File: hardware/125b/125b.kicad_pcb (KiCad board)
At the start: 2 copper layers, 59 x 75 mm, 49 parts, among them J1 Guitar in, J2 Barrel_Jack, J3 Conn_02x05_Odd_Even_MountingP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, J4 Guitar out, SW1 SW_Push_SPDT, SW2 RotaryEncoder_Switch, SW3 SW_Push, SW4 SW_Push, U1 L78L05_TO92, U2 TL074

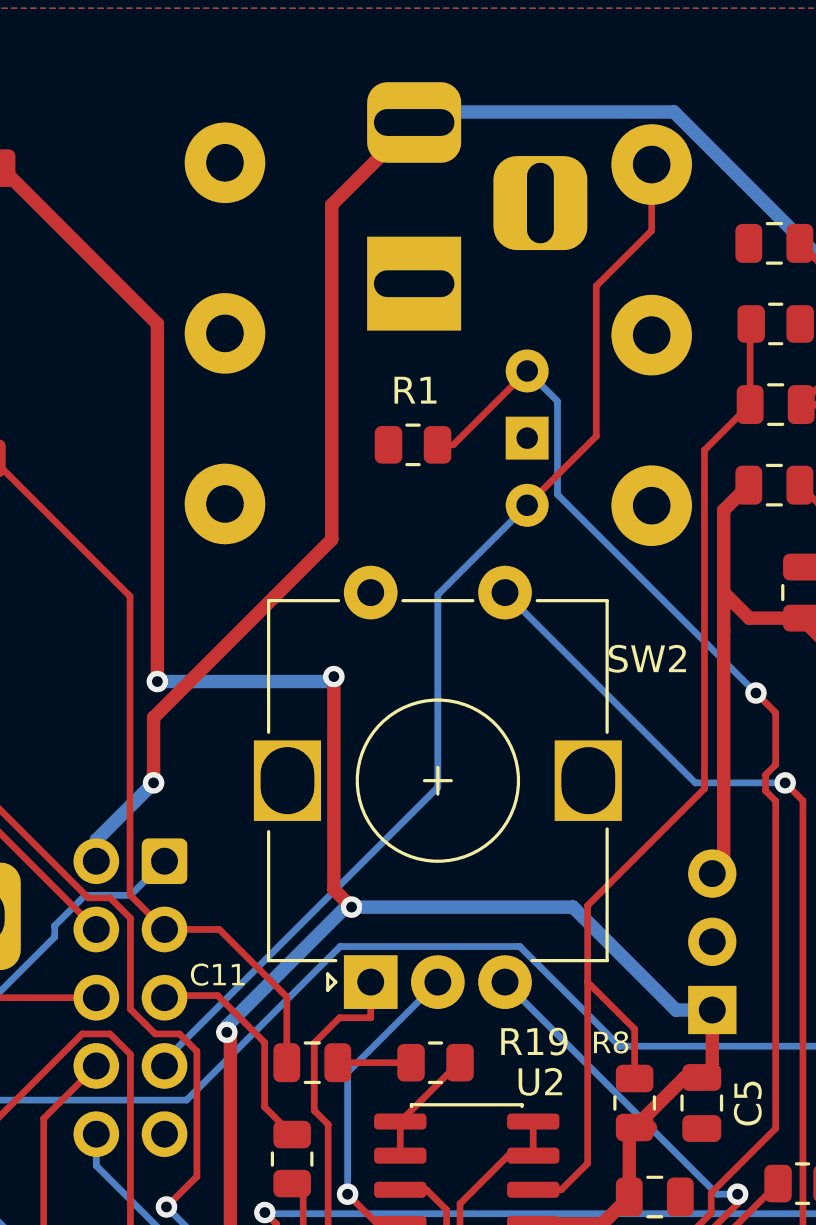
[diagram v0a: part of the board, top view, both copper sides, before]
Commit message: Fix line in switch footprint and update pcb
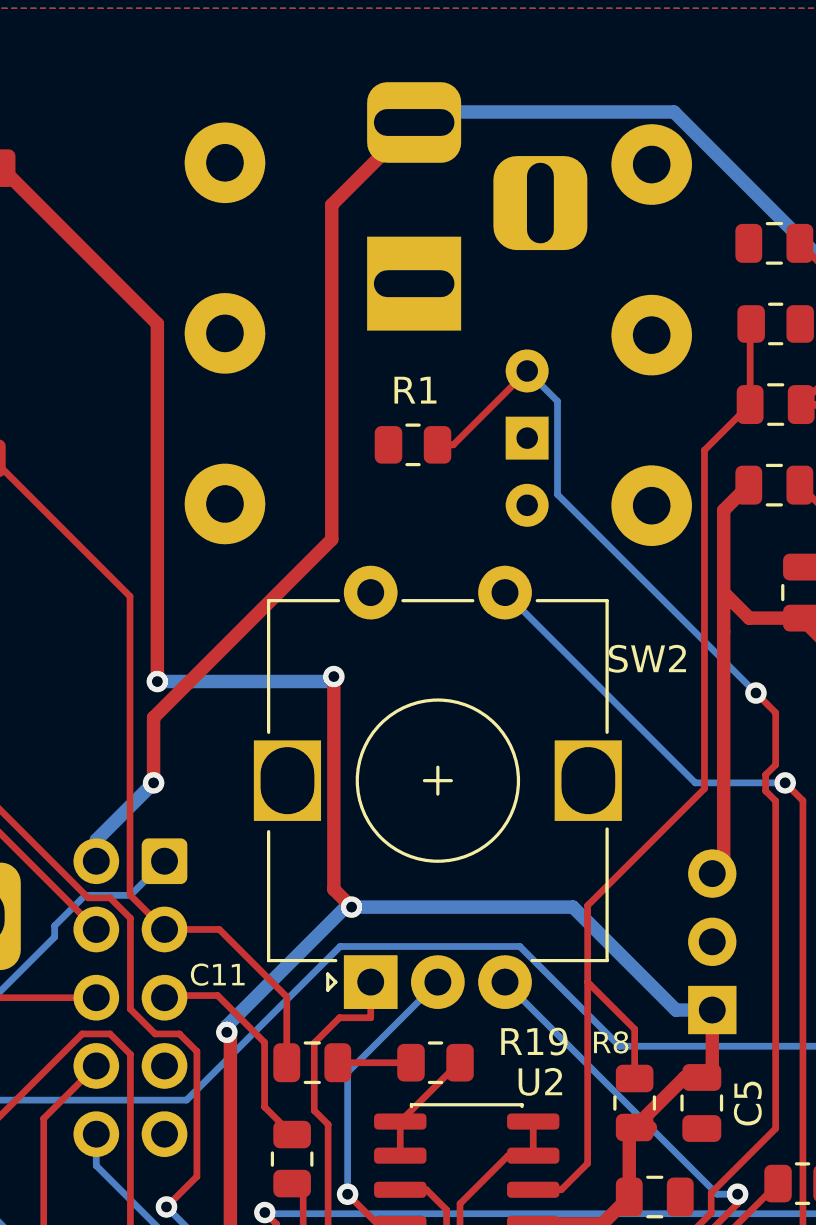
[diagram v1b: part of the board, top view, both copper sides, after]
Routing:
- net /fsw7: track 41.1 -> 0.20 mm
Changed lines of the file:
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@@
 			(pintype "passive")
 		)
-		(pad "2" thru_hole circle
-			(at 0 -1.6 90)
+		(pad "2" thru_hole rect
+			(at 2.5 -1.6 90)
 			(size 1.6 1.6)
 			(drill 0.8)
@@
 			(pintype "passive")
 		)
-		(pad "C" thru_hole rect
-			(at 2.5 -1.6 90)
+		(pad "3" thru_hole circle
+			(at 0 -1.6 90)
 			(size 1.6 1.6)
 			(drill 0.8)
 			(layers "*.Cu" "*.Mask")
 			(remove_unused_layers no)
+			(net 16 "/Left in")
+			(pinfunction "C")
+			(pintype "passive")
 		)
 		(embedded_fonts no)
@@
 	)
 	(segment
-		(start 135.385 44.0258)
-		(end 135.385 41.565)
-		(width 0.25)
-		(layer "F.Cu")
-		(net 48)
-	)
-	(segment
-		(start 133.321 51.679)
-		(end 133.321 46.0898)
-		(width 0.25)
-		(layer "F.Cu")
-		(net 48)
-	)
-	(segment
-		(start 130.75 54.25)
-		(end 133.321 51.679)
-		(width 0.25)
-		(layer "F.Cu")
-		(net 48)
-	)
-	(segment
-		(start 133.321 46.0898)
-		(end 135.385 44.0258)
-		(width 0.25)
-		(layer "F.Cu")
-		(net 48)
-	)
-	(segment
-		(start 130.75 54.25)
-		(end 127.4251 57.5749)
-		(width 0.25)
-		(layer "B.Cu")
-		(net 48)
-	)
-	(segment
-		(start 127.4251 57.5749)
-		(end 127.4251 64.7464)
-		(width 0.25)
-		(layer "B.Cu")
-		(net 48)
-	)
-	(segment
 		(start 117.25 74.9215)
 		(end 117.25 75.12)
 		(width 0.25)
 		(layer "B.Cu")
-		(net 48)
-	)
-	(segment
-		(start 127.4251 64.7464)
-		(end 117.25 74.9215)
-		(width 0.25)
-		(layer "B.Cu")

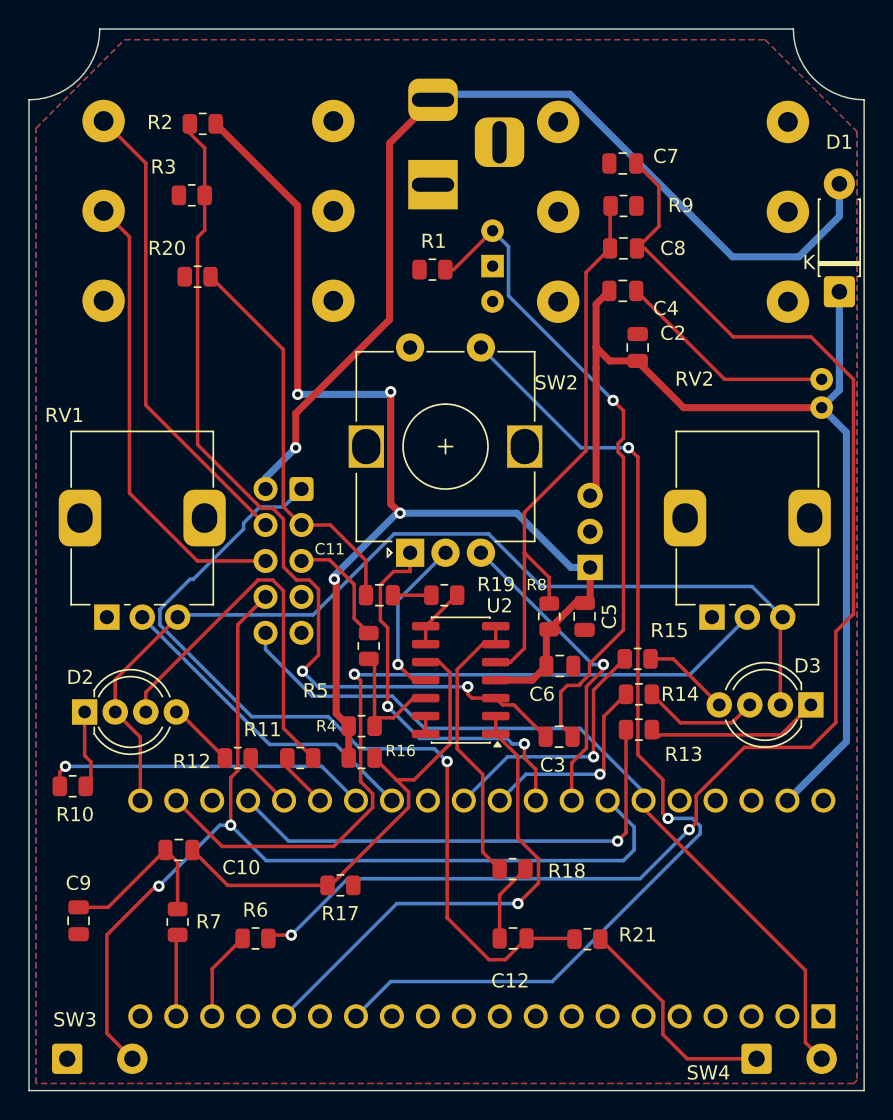
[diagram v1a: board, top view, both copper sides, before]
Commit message: Rotate the audio sockets (and correct the 3d model orientation)
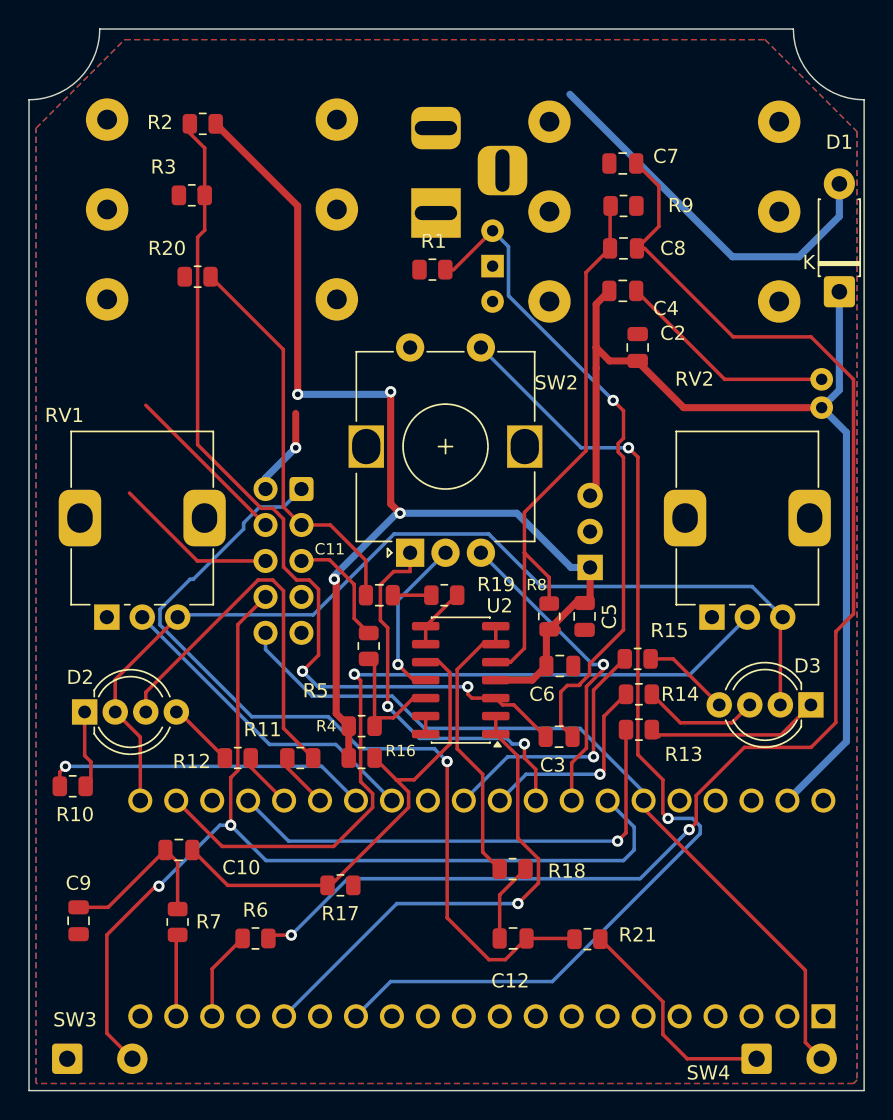
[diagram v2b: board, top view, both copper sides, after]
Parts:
- moved J4 20.7 mm to (119.8, 54.1), turned to 90 degrees
- moved J1 20.1 mm to (151.0, 54.2), turned to 90 degrees
- moved J2 2.01 mm to (126.8, 48.0)
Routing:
- net /fsw2: track 69.5 -> 33.5 mm
- net /fsw4: track 33.3 -> 12.0 mm
- net /fsw6: track 32.3 -> 11.6 mm

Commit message: Update version number on board
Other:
- board text added: "Prog1 v0.7 Denis Crowdy, Prog Pedals"
- board text removed: "Prog1 v0.6 Denis Crowdy, Prog Pedals"
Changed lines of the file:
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@@
 		(layer "Edge.Cuts")
 	)
-	(gr_text "Prog1 v0.6 Denis Crowdy, Prog Pedals"
+	(gr_text "Prog1 v0.7 Denis Crowdy, Prog Pedals"
 		(at 142 108.45 0)
 		(layer "B.SilkS")

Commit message: Reconnect, adjust some positions, and tweak
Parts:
- moved R2 43.1 mm to (117.2, 84.2)
- moved R3 10.0 mm to (110.3, 56.8)
- moved SW1 7.75 mm to (124.8, 55.8), turned to 0 degrees
- moved C4 4.99 mm to (143.5, 50.0)
- moved C8 4.96 mm to (143.2, 46.8), turned to 0 degrees
- moved C7 2.55 mm to (138.8, 46.8)
- moved R9 2.15 mm to (138.8, 49.2), turned to 180 degrees
- moved R20 1.56 mm to (110.3, 54.0)
- moved R1 0.75 mm to (126.5, 51.2)
- moved J2 0.25 mm to (126.5, 48.0)
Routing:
- net /Left in: track 34.9 -> 134.7 mm
- net /fsw7: track 0.20 -> 50.7 mm
- net /fsw2: track 33.5 -> 69.0 mm
- net +5V: track 85.2 -> 50.4 mm, vias 4 -> 1
- net /fsw6: track 11.6 -> 31.2 mm
- net Net-(C7-Pad2): track 98.7 -> 110.3 mm
- net Net-(U2A-+): track 64.3 -> 55.0 mm
- net GND: track 51.7 -> 42.8 mm
- net /fsw4: track 12.0 -> 19.2 mm
- net /VCC: track 71.7 -> 76.7 mm
- net Net-(SW1-A): track 47.7 -> 43.4 mm
- net Net-(U2B-+): track 40.5 -> 44.6 mm
- net Net-(D2-GK): track 27.4 -> 28.5 mm
- net /fsw1: track 61.1 -> 61.8 mm

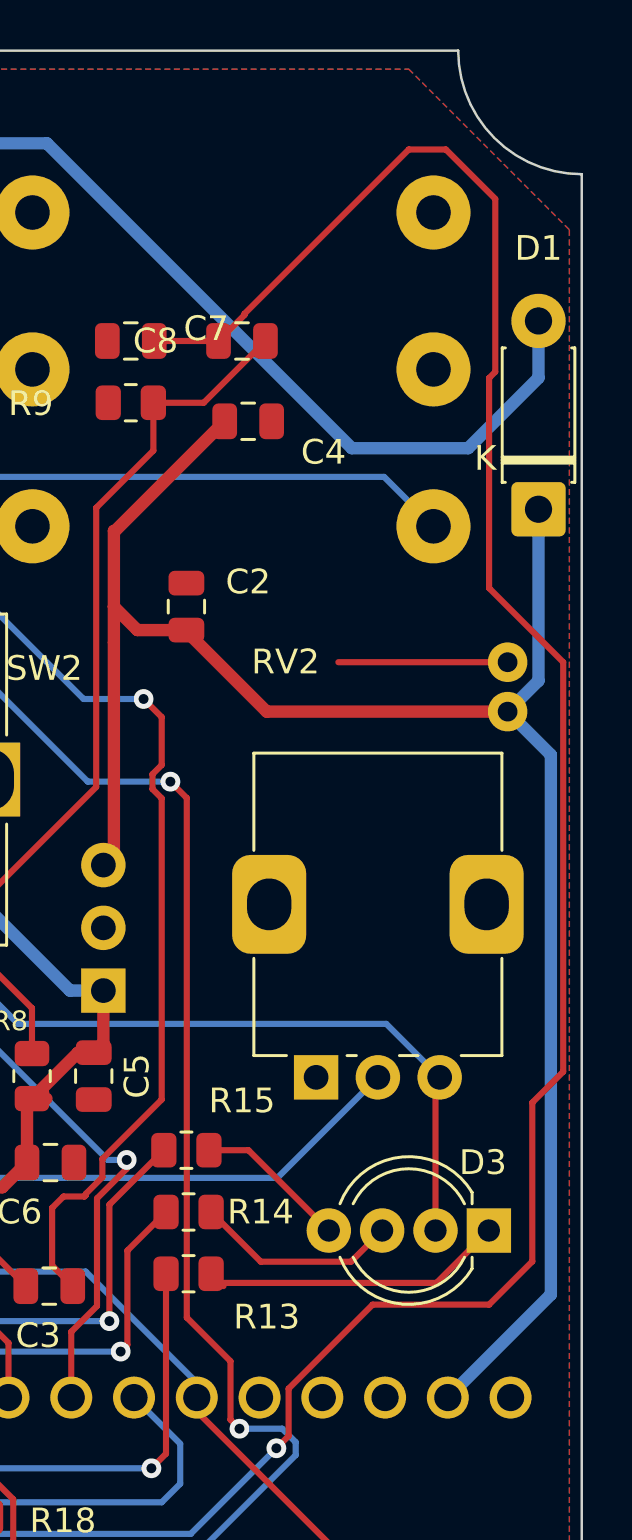
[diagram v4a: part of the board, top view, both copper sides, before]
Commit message: Put D2 and D3 in same y position
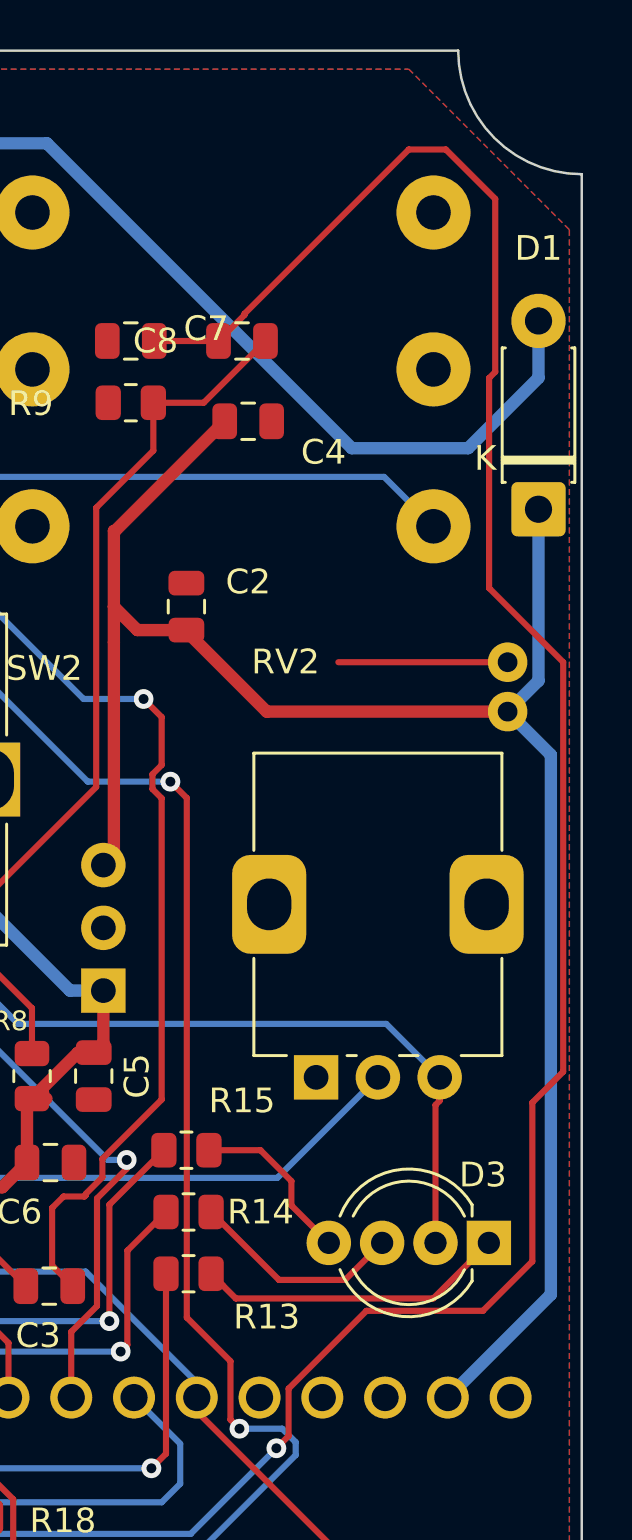
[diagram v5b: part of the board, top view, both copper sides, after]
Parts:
- moved D3 0.50 mm to (153.2, 83.2)
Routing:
- net Net-(D3-BK): track 6.20 -> 6.98 mm
- net /3v3: track 69.4 -> 70.1 mm
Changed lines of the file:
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@@
 	(footprint "LED_THT:LED_D5.0mm-4_RGB_Wide_Pins"
 		(layer "F.Cu")
-		(at 153.24 82.75 180)
+		(at 153.24 83.25 180)
 		(descr "LED, diameter 5.0mm, 4 pins, WP154A4, https://www.kingbright.com/attachments/file/psearch/000/00/00/L-154A4SUREQBFZGEW(Ver.11A).pdf")
 		(tags "LED diameter 5.0mm 2 pins diameter 5.0mm 3 pins diameter 5.0mm 4 pins RGB RGBLED")
@@
 	)
 	(segment
+		(start 151.081 77.669)
+		(end 151.081 83.25)
+		(width 0.25)
+		(layer "F.Cu")
+		(net 21)
+	)
+	(segment
 		(start 105.86 85.019)
 		(end 104.091 83.25)
@@
 	)
 	(segment
-		(start 151.081 82.75)
-		(end 151.081 76.719)
+		(start 151.25 76.55)
+		(end 151.25 77.5)
+		(width 0.25)
+		(layer "F.Cu")
+		(net 21)
+	)
+	(segment
+		(start 151.25 77.5)
+		(end 151.081 77.669)
 		(width 0.25)
 		(layer "F.Cu")
@@
 	)
 	(segment
-		(start 142 84.5)
-		(end 142.37 84.87)
+		(start 150.99 85.5)
+		(end 153.24 83.25)
 		(width 0.25)
 		(layer "F.Cu")
@@
 	)
 	(segment
-		(start 151.12 84.87)
-		(end 153.24 82.75)
+		(start 143 85.5)
+		(end 150.99 85.5)
 		(width 0.25)
 		(layer "F.Cu")
@@
 	)
 	(segment
-		(start 142.5 85)
-		(end 142 84.5)
+		(start 142 84.5)
+		(end 143 85.5)
 		(width 0.25)
 		(layer "F.Cu")
@@
 	)
 	(segment
-		(start 142.37 84.87)
-		(end 151.12 84.87)
+		(start 142.5 85)
+		(end 142 84.5)
 		(width 0.25)
 		(layer "F.Cu")
@@
 	(segment
 		(start 142 82)
-		(end 144.0125 84.0125)
+		(end 144.75 84.75)
 		(width 0.25)
 		(layer "F.Cu")
@@
 	)
 	(segment
-		(start 144.0125 84.0125)
-		(end 147.6595 84.0125)
+		(start 147.422 84.75)
+		(end 148.922 83.25)
 		(width 0.25)
 		(layer "F.Cu")
@@
 	)
 	(segment
-		(start 147.6595 84.0125)
-		(end 148.922 82.75)
+		(start 144.75 84.75)
+		(end 147.422 84.75)
 		(width 0.25)
 		(layer "F.Cu")
@@
 	)
 	(segment
-		(start 143.513 79.5)
-		(end 146.763 82.75)
+		(start 145.25 80.75)
+		(end 145.25 81.737)
+		(width 0.25)
+		(layer "F.Cu")
+		(net 43)
+	)
+	(segment
+		(start 144 79.5)
+		(end 145.25 80.75)
 		(width 0.25)
 		(layer "F.Cu")
@@
 	(segment
 		(start 141.9125 79.5)
-		(end 143.513 79.5)
+		(end 144 79.5)
+		(width 0.25)
+		(layer "F.Cu")
+		(net 43)
+	)
+	(segment
+		(start 145.25 81.737)
+		(end 146.763 83.25)
 		(width 0.25)
 		(layer "F.Cu")
@@
 	)
 	(segment
-		(start 153.25 56.75)
-		(end 153.25 48.25)
-		(width 0.25)
-		(layer "F.Cu")
-		(net 54)
-	)
-	(segment
-		(start 153.25 85.75)
+		(start 153 86)
 		(end 155 84)
 		(width 0.25)
@@
 	)
 	(segment
-		(start 155 77.5723)
-		(end 156.25 76.3223)
+		(start 115.1475 99.015)
+		(end 114.9125 99.25)
 		(width 0.25)
 		(layer "F.Cu")
@@
 	(segment
 		(start 150 39)
-		(end 151.5 39)
+		(end 143.351 45.649)
 		(width 0.25)
 		(layer "F.Cu")
@@
 	)
 	(segment
-		(start 115.1475 99.015)
-		(end 114.9125 99.25)
+		(start 153.25 56.75)
+		(end 153.25 48.25)
 		(width 0.25)
 		(layer "F.Cu")
@@
 	)
 	(segment
-		(start 153.5 41)
-		(end 153.5 48)
+		(start 145.1367 91.0659)
+		(end 145.1367 89.1499)
 		(width 0.25)
 		(layer "F.Cu")
@@
 	)
 	(segment
-		(start 143.351 45.699)
-		(end 143.351 45.649)
+		(start 143.351 45.649)
+		(end 143.351 45.699)
 		(width 0.25)
 		(layer "F.Cu")
@@
 	)
 	(segment
-		(start 153.5 48)
-		(end 153.25 48.25)
+		(start 144.6408 91.5618)
+		(end 145.1367 91.0659)
 		(width 0.25)
 		(layer "F.Cu")
@@
 	)
 	(segment
-		(start 143.351 45.649)
-		(end 150 39)
+		(start 155 84)
+		(end 155 77.5723)
 		(width 0.25)
 		(layer "F.Cu")
@@
 	(segment
 		(start 145.1367 89.1499)
-		(end 148.5366 85.75)
+		(end 148.2866 86)
 		(width 0.25)
 		(layer "F.Cu")
@@
 	)
 	(segment
-		(start 142.3 46.75)
-		(end 143.351 45.699)
+		(start 139.7 46.75)
+		(end 142.3 46.75)
 		(width 0.25)
 		(layer "F.Cu")
@@
 	(segment
 		(start 151.5 39)
-		(end 153.5 41)
+		(end 150 39)
 		(width 0.25)
 		(layer "F.Cu")
@@
 	)
 	(segment
-		(start 148.5366 85.75)
-		(end 153.25 85.75)
+		(start 156.25 59.75)
+		(end 153.25 56.75)
 		(width 0.25)
 		(layer "F.Cu")
@@
 	)
 	(segment
-		(start 156.25 59.75)
-		(end 153.25 56.75)
+		(start 148.2866 86)
+		(end 153 86)
 		(width 0.25)
 		(layer "F.Cu")
@@
 	)
 	(segment
-		(start 155 84)
-		(end 155 77.5723)
+		(start 143.351 45.699)
+		(end 142.3 46.75)
 		(width 0.25)
 		(layer "F.Cu")
@@
 	)
 	(segment
-		(start 139.7 46.75)
-		(end 142.3 46.75)
+		(start 116.5298 99.015)
+		(end 115.1475 99.015)
 		(width 0.25)
 		(layer "F.Cu")
@@
 	)
 	(segment
-		(start 145.1367 91.0659)
-		(end 145.1367 89.1499)
+		(start 153.5 48)
+		(end 153.5 41)
 		(width 0.25)
 		(layer "F.Cu")
@@
 	)
 	(segment
-		(start 144.6408 91.5618)
-		(end 145.1367 91.0659)
+		(start 153.5 41)
+		(end 151.5 39)
 		(width 0.25)
 		(layer "F.Cu")
@@
 	)
 	(segment
-		(start 116.5298 99.015)
-		(end 115.1475 99.015)
+		(start 155 77.5723)
+		(end 156.25 76.3223)
 		(width 0.25)
 		(layer "F.Cu")
@@
 		(width 0.25)
 		(layer "F.Cu")
+		(net 54)
+	)
+	(segment
+		(start 153.25 48.25)
+		(end 153.5 48)
+		(width 0.25)
+		(layer "F.Cu")
